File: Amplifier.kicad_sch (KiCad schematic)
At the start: 62 parts, among them Q301 PNP, Q302 NPN, Q303 PNP, Q304 NPN, Q305 NPN, Q306 PNP, Q307 NPN, Q308 PNP, Q309 PNP, Q310 NPN, Q311 PNP, Q312 NPN, Q313 PNP, Q314 NPN, Q315 PNP, Q316 NPN, Q317 NPN, Q318 PNP, Q319 NPN, Q320 PNP, Q321 PNP, Q322 NPN, Q323 PNP, Q324 NPN, U301 ???, U302 ???

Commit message: 回路図ひとまず完成
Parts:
- removed Q301, Q303, Q308, Q320, Q321, Q323: PNP, Package_TO_SOT_THT:TO-92L_Inline_Wide, symbol Transistor_BJT:Q_PNP_ECB
- removed Q304, Q305, Q307, Q317, Q319, Q324: NPN, Package_TO_SOT_THT:TO-92L_Inline_Wide, symbol Transistor_BJT:Q_NPN_ECB
- removed RV301, RV302: 10k, MyLibrary:SL4515G, symbol MysymbolLibrary:RV_2C
- added Q401, Q402, Q411, Q412, Q417, Q418: TPC6901A, symbol MysymbolLibrary:TPC6901A
- added RV401: R, MyLibrary:RV_2C, symbol MysymbolLibrary:RV_2C
- renumbered C302 to C401, C301 to C402, HS301 to HS401, HS303 to HS402, HS302 to HS403, HS304 to HS404, Q309 to Q403, Q313 to Q404, Q302 to Q405, Q322 to Q406, Q306 to Q407, Q318 to Q408, Q310 to Q409, Q314 to Q410, Q311 to Q413, Q315 to Q414, Q312 to Q415, Q316 to Q416, R307 to R401, R319 to R402, R311 to R403, R315 to R404, R312 to R405, R316 to R406, R305 to R407, R323 to R408, R308 to R409, R320 to R410, R303 to R411, R325 to R412, R301 to R413, R328 to R414, R306 to R415, R324 to R416, R302 to R417, R327 to R418, R309 to R419, R321 to R420, R304 to R421, R326 to R422, R313 to R423, R317 to R424, R314 to R425, R318 to R426, R310 to R427, R322 to R428, U301 to U401, U302 to U402
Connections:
- net EQ_L: now also RV401.1
- net EQ_R: now also RV401.4
- net GNDREF: now also RV401.3, RV401.6
- net V+: now also Q417.6, Q418.6
- net V-: now also Q401.4, Q402.4, Q411.4, Q412.4
- net at Q414.2 (C), R424.1: now also Q412.5
- net at R401.2: now also Q401.1, Q401.2
- net at R419.2: now also Q411.1, Q411.2
- net at R414.1, U402.5 (+): now also RV401.5
- net at Q406.3 (B), R408.2, U402.7: now also Q402.3
- net at Q416.2 (C), R426.2: now also Q418.2
- net at Q416.3 (B): now also Q418.4
- net at Q405.3 (B), R407.2, U401.7: now also Q401.3
- net at Q415.2 (C), R425.2: now also Q417.2
- net at Q413.2 (C), R423.1: now also Q411.5
- net at R416.2, U402.8: now also Q412.3, Q418.1
- net at R402.2: now also Q402.1, Q402.2
- net at Q404.2 (C), R404.1: now also Q402.5
- net at Q404.3 (B): now also Q402.6
- net at R428.1: now also Q418.3, Q418.5
- net at Q403.2 (C), R403.1: now also Q401.5
- net at Q403.3 (B): now also Q401.6
- net at Q415.3 (B): now also Q417.4
- net at Q413.3 (B): now also Q411.6
- net at R413.1, U401.5 (+): now also RV401.2
- net at Q414.3 (B): now also Q412.6
- net at R415.2, U401.8: now also Q411.3, Q417.1
- net at R427.1: now also Q417.3, Q417.5
- net at R420.2: now also Q412.1, Q412.2

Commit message: Amplifier回路図更新
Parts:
- removed Q405, Q406: NPN, Package_TO_SOT_THT:TO-92L_Inline_Wide, symbol Transistor_BJT:Q_NPN_ECB
- removed Q407, Q408: PNP, Package_TO_SOT_THT:TO-92L_Inline_Wide, symbol Transistor_BJT:Q_PNP_ECB
- added Q407, Q408: TPC6901A, symbol MysymbolLibrary:TPC6901A
- renumbered Q409 to Q405, Q410 to Q406, Q411 to Q409, Q412 to Q410, Q413 to Q411, Q414 to Q412, Q415 to Q413, Q416 to Q414, Q417 to Q415, Q418 to Q416
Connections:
- net V+: now also Q407.6, Q408.6
- net at Q402.3, R408.2, U402.7: now also Q408.1
- net at Q406.2 (C), R406.2: now also Q408.2
- net at Q406.3 (B): now also Q408.4
- net at R410.1: now also Q408.3, Q408.5
- net at Q401.3, R407.2, U401.7: now also Q407.1
- net at R409.1: now also Q407.3, Q407.5
- net at Q405.2 (C), R405.2: now also Q407.2
- net at Q405.3 (B): now also Q407.4

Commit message: 部品ほぼ割り当て
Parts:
- C401, C402: footprint (none) -> Capacitor_SMD:C_1206_3216Metric
- HS401, HS402, HS403, HS404: footprint (none) -> MyLibrary:17PB024
- Q401, Q402, Q407, Q408, Q409, Q410, Q415, Q416: footprint (none) -> Package_TO_SOT_SMD:SOT-23-6
- Q403, Q404, Q405, Q406, Q411, Q412, Q413, Q414: footprint Package_TO_SOT_THT:TO-92L_Inline_Wide -> Package_TO_SOT_THT:TO-126-3_Vertical
- R401, R402, R409, R410, R419, R420, R427, R428: footprint Resistor_THT:R_Axial_DIN0204_L3.6mm_D1.6mm_P5.08mm_Horizontal -> Resistor_SMD:R_2512_6332Metric
- R407, R408, R411, R412, R413, R414, R415, R416, R417, R418, R421, R422: footprint Resistor_THT:R_Axial_DIN0204_L3.6mm_D1.6mm_P5.08mm_Horizontal -> Resistor_SMD:R_0603_1608Metric
- U401, U402: footprint (none) -> Package_DIP:DIP-14_W7.62mm_Socket
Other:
- note added: "ヒートシンク"
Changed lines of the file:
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@@
 		)
 	)
+	(text "ヒートシンク"
+		(exclude_from_sim no)
+		(at 271.78 74.168 0)
+		(effects
+			(font
+				(size 1.27 1.27)
+			)
+			(href "https://akizukidenshi.com/catalog/g/g105049/")
+		)
+	)
 	(text "Rd"
 		(exclude_from_sim no)
@@
 			)
 		)
-		(property "Footprint" "Resistor_THT:R_Axial_DIN0204_L3.6mm_D1.6mm_P5.08mm_Horizontal"
+		(property "Footprint" "Resistor_SMD:R_2512_6332Metric"
 			(at 108.712 43.18 90)
 			(hide yes)
@@
 			)
 		)
-		(property "Footprint" "Resistor_THT:R_Axial_DIN0204_L3.6mm_D1.6mm_P5.08mm_Horizontal"
+		(property "Footprint" "Resistor_SMD:R_0603_1608Metric"
 			(at 76.708 106.68 90)
 			(hide yes)
@@
 			)
 		)
-		(property "Footprint" "Resistor_THT:R_Axial_DIN0204_L3.6mm_D1.6mm_P5.08mm_Horizontal"
+		(property "Footprint" "Resistor_SMD:R_2512_6332Metric"
 			(at 108.712 105.41 90)
 			(hide yes)
@@
 			)
 		)
-		(property "Footprint" ""
+		(property "Footprint" "Package_DIP:DIP-14_W7.62mm_Socket"
 			(at 251.46 25.4 0)
 			(hide yes)
@@
 			)
 		)
-		(property "Footprint" ""
+		(property "Footprint" "Package_DIP:DIP-14_W7.62mm_Socket"
 			(at 276.86 25.4 0)
 			(hide yes)
@@
 			)
 		)
-		(property "Footprint" ""
+		(property "Footprint" "Package_DIP:DIP-14_W7.62mm_Socket"
 			(at 213.36 80.01 0)
 			(hide yes)
@@
 			)
 		)
-		(property "Footprint" "Package_TO_SOT_THT:TO-92L_Inline_Wide"
+		(property "Footprint" "Package_TO_SOT_THT:TO-126-3_Vertical"
 			(at 161.29 138.43 0)
 			(hide yes)
@@
 			)
 		)
-		(property "Footprint" "Resistor_THT:R_Axial_DIN0204_L3.6mm_D1.6mm_P5.08mm_Horizontal"
+		(property "Footprint" "Resistor_SMD:R_0603_1608Metric"
 			(at 76.708 82.55 90)
 			(hide yes)
@@
 			)
 		)
-		(property "Footprint" ""
+		(property "Footprint" "Package_DIP:DIP-14_W7.62mm_Socket"
 			(at 58.42 106.68 0)
 			(hide yes)
@@
 			)
 		)
-		(property "Footprint" "Resistor_THT:R_Axial_DIN0204_L3.6mm_D1.6mm_P5.08mm_Horizontal"
+		(property "Footprint" "Resistor_SMD:R_0603_1608Metric"
 			(at 213.36 98.298 90)
 			(hide yes)
@@
 			)
 		)
-		(property "Footprint" ""
+		(property "Footprint" "Package_TO_SOT_SMD:SOT-23-6"
 			(at 124.46 82.55 0)
 			(hide yes)
@@
 			)
 		)
-		(property "Footprint" "Resistor_THT:R_Axial_DIN0204_L3.6mm_D1.6mm_P5.08mm_Horizontal"
+		(property "Footprint" "Resistor_SMD:R_0603_1608Metric"
 			(at 221.742 106.68 90)
 			(hide yes)
@@
 			)
 		)
-		(property "Footprint" "Package_TO_SOT_THT:TO-92L_Inline_Wide"
+		(property "Footprint" "Package_TO_SOT_THT:TO-126-3_Vertical"
 			(at 161.29 45.72 0)
 			(hide yes)
@@
 			)
 		)
-		(property "Footprint" "Resistor_THT:R_Axial_DIN0204_L3.6mm_D1.6mm_P5.08mm_Horizontal"
+		(property "Footprint" "Resistor_SMD:R_2512_6332Metric"
 			(at 184.658 140.97 90)
 			(hide yes)
@@
 			)
 		)
-		(property "Footprint" ""
+		(property "Footprint" "Package_TO_SOT_SMD:SOT-23-6"
 			(at 110.49 101.6 0)
 			(hide yes)
@@
 			)
 		)
-		(property "Footprint" ""
+		(property "Footprint" "Package_TO_SOT_SMD:SOT-23-6"
 			(at 124.46 144.78 0)
 			(hide yes)
@@
 			)
 		)
-		(property "Footprint" "Package_TO_SOT_THT:TO-92L_Inline_Wide"
+		(property "Footprint" "Package_TO_SOT_THT:TO-126-3_Vertical"
 			(at 132.08 45.72 0)
 			(hide yes)
@@
 			)
 		)
-		(property "Footprint" ""
+		(property "Footprint" "Package_TO_SOT_SMD:SOT-23-6"
 			(at 110.49 39.37 0)
 			(hide yes)
@@
 			)
 		)
-		(property "Footprint" "Package_TO_SOT_THT:TO-92L_Inline_Wide"
+		(property "Footprint" "Package_TO_SOT_THT:TO-126-3_Vertical"
 			(at 132.08 138.43 0)
 			(hide yes)
@@
 			)
 		)
-		(property "Footprint" "Package_TO_SOT_THT:TO-92L_Inline_Wide"
+		(property "Footprint" "Package_TO_SOT_THT:TO-126-3_Vertical"
 			(at 132.08 107.95 0)
 			(hide yes)
@@
 			)
 		)
-		(property "Footprint" "Resistor_THT:R_Axial_DIN0204_L3.6mm_D1.6mm_P5.08mm_Horizontal"
+		(property "Footprint" "Resistor_SMD:R_0603_1608Metric"
 			(at 221.742 82.55 90)
 			(hide yes)
@@
 			)
 		)
-		(property "Footprint" "Resistor_THT:R_Axial_DIN0204_L3.6mm_D1.6mm_P5.08mm_Horizontal"
+		(property "Footprint" "Resistor_SMD:R_0603_1608Metric"
 			(at 85.09 74.168 90)
 			(hide yes)
@@
 			)
 		)
-		(property "Footprint" "Resistor_THT:R_Axial_DIN0204_L3.6mm_D1.6mm_P5.08mm_Horizontal"
+		(property "Footprint" "Resistor_SMD:R_0603_1608Metric"
 			(at 52.578 93.98 90)
 			(hide yes)
@@
 			)
 		)
-		(property "Footprint" "Package_TO_SOT_THT:TO-92L_Inline_Wide"
+		(property "Footprint" "Package_TO_SOT_THT:TO-126-3_Vertical"
 			(at 161.29 107.95 0)
 			(hide yes)
@@
 			)
 		)
-		(property "Footprint" ""
+		(property "Footprint" "Package_DIP:DIP-14_W7.62mm_Socket"
 			(at 248.92 49.53 0)
 			(hide yes)
@@
 			)
 		)
-		(property "Footprint" "Resistor_THT:R_Axial_DIN0204_L3.6mm_D1.6mm_P5.08mm_Horizontal"
+		(property "Footprint" "Resistor_SMD:R_0603_1608Metric"
 			(at 240.03 100.838 90)
 			(hide yes)
@@
 			)
 		)
-		(property "Footprint" "Package_TO_SOT_THT:TO-92L_Inline_Wide"
+		(property "Footprint" "Package_TO_SOT_THT:TO-126-3_Vertical"
 			(at 161.29 76.2 0)
 			(hide yes)
@@
 			)
 		)
-		(property "Footprint" ""
+		(property "Footprint" "Package_TO_SOT_SMD:SOT-23-6"
 			(at 182.88 39.37 0)
 			(hide yes)
@@
 			)
 		)
-		(property "Footprint" ""
+		(property "Footprint" "Package_TO_SOT_SMD:SOT-23-6"
 			(at 182.88 101.6 0)
 			(hide yes)
@@
 			)
 		)
-		(property "Footprint" ""
+		(property "Footprint" "MyLibrary:17PB024"
 			(at 269.5448 69.85 0)
 			(hide yes)
@@
 			)
 		)
-		(property "Footprint" "Resistor_THT:R_Axial_DIN0204_L3.6mm_D1.6mm_P5.08mm_Horizontal"
+		(property "Footprint" "Resistor_SMD:R_0603_1608Metric"
 			(at 213.36 74.168 90)
 			(hide yes)
@@
 			)
 		)
-		(property "Footprint" "Resistor_THT:R_Axial_DIN0204_L3.6mm_D1.6mm_P5.08mm_Horizontal"
+		(property "Footprint" "Resistor_SMD:R_0603_1608Metric"
 			(at 85.09 98.298 90)
 			(hide yes)
@@
 			)
 		)
-		(property "Footprint" ""
+		(property "Footprint" "MyLibrary:17PB024"
 			(at 251.7648 69.85 0)
 			(hide yes)
@@
 			)
 		)
-		(property "Footprint" ""
+		(property "Footprint" "Package_TO_SOT_SMD:SOT-23-6"
 			(at 168.91 144.78 0)
 			(hide yes)
@@
 			)
 		)
-		(property "Footprint" "Resistor_THT:R_Axial_DIN0204_L3.6mm_D1.6mm_P5.08mm_Horizontal"
+		(property "Footprint" "Resistor_SMD:R_0603_1608Metric"
 			(at 58.42 100.838 90)
 			(hide yes)
@@
 			)
 		)
-		(property "Footprint" ""
+		(property "Footprint" "Package_DIP:DIP-14_W7.62mm_Socket"
 			(at 240.03 106.68 0)
 			(hide yes)
@@
 			)
 		)
-		(property "Footprint" "Resistor_THT:R_Axial_DIN0204_L3.6mm_D1.6mm_P5.08mm_Horizontal"
+		(property "Footprint" "Resistor_SMD:R_2512_6332Metric"
 			(at 184.658 43.18 90)
 			(hide yes)
@@
 			)
 		)
-		(property "Footprint" ""
+		(property "Footprint" "Capacitor_SMD:C_1206_3216Metric"
 			(at 246.0752 29.21 0)
 			(hide yes)
@@
 			)
 		)
-		(property "Footprint" "Resistor_THT:R_Axial_DIN0204_L3.6mm_D1.6mm_P5.08mm_Horizontal"
+		(property "Footprint" "Resistor_SMD:R_2512_6332Metric"
 			(at 184.658 78.74 90)
 			(hide yes)
@@
 			)
 		)
-		(property "Footprint" "Resistor_THT:R_Axial_DIN0204_L3.6mm_D1.6mm_P5.08mm_Horizontal"
+		(property "Footprint" "Resistor_SMD:R_2512_6332Metric"
 			(at 108.712 78.74 90)
 			(hide yes)
@@
 			)
 		)
-		(property "Footprint" ""
+		(property "Footprint" "Package_DIP:DIP-14_W7.62mm_Socket"
 			(at 213.36 104.14 0)
 			(hide yes)
@@
 			)
 		)
-		(property "Footprint" "Resistor_THT:R_Axial_DIN0204_L3.6mm_D1.6mm_P5.08mm_Horizontal"
+		(property "Footprint" "Resistor_SMD:R_2512_6332Metric"
 			(at 108.712 140.97 90)
 			(hide yes)
@@
 			)
 		)
-		(property "Footprint" ""
+		(property "Footprint" "MyLibrary:17PB024"
 			(at 251.7648 64.77 0)
 			(hide yes)
@@
 			)
 		)
-		(property "Footprint" ""
+		(property "Footprint" "Capacitor_SMD:C_1206_3216Metric"
 			(at 271.4752 29.21 0)
 			(hide yes)
@@
 			)
 		)
-		(property "Footprint" ""
+		(property "Footprint" "Package_DIP:DIP-14_W7.62mm_Socket"
 			(at 274.32 49.53 0)
 			(hide yes)
@@
 			)
 		)
-		(property "Footprint" "Resistor_THT:R_Axial_DIN0204_L3.6mm_D1.6mm_P5.08mm_Horizontal"
+		(property "Footprint" "Resistor_SMD:R_2512_6332Metric"
 			(at 184.658 105.41 90)
 			(hide yes)
@@
 			)
 		)
-		(property "Footprint" ""
+		(property "Footprint" "Package_TO_SOT_SMD:SOT-23-6"
 			(at 168.91 82.55 0)
 			(hide yes)
@@
 			)
 		)
-		(property "Footprint" ""
+		(property "Footprint" "Package_DIP:DIP-14_W7.62mm_Socket"
 			(at 85.09 80.01 0)
 			(hide yes)
@@
 			)
 		)
-		(property "Footprint" ""
+		(property "Footprint" "Package_DIP:DIP-14_W7.62mm_Socket"
 			(at 85.09 104.14 0)
 			(hide yes)
@@
 			)
 		)
-		(property "Footprint" ""
+		(property "Footprint" "MyLibrary:17PB024"
 			(at 269.5448 64.77 0)
 			(hide yes)
@@
 			)
 		)
-		(property "Footprint" "Package_TO_SOT_THT:TO-92L_Inline_Wide"
+		(property "Footprint" "Package_TO_SOT_THT:TO-126-3_Vertical"
 			(at 132.08 76.2 0)
 			(hide yes)
@@
 			)
 		)
-		(property "Footprint" "Resistor_THT:R_Axial_DIN0204_L3.6mm_D1.6mm_P5.08mm_Horizontal"
+		(property "Footprint" "Resistor_SMD:R_0603_1608Metric"
 			(at 245.872 93.98 90)
 			(hide yes)

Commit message: 部品配置すすめた
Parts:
- removed HS401, HS402, HS403, HS404: Heatsink, MyLibrary:17PB024, symbol Mechanical:Heatsink
- Q403, Q404, Q411, Q412: value PNP -> 2SA1359
- Q405, Q406, Q413, Q414: value NPN -> 2SC3422
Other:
- note added: "100~200mAくらい"
- note added: "やっぱヒートシンクこれで 長い一体のもの，8℃/W ダメだったら空冷で"

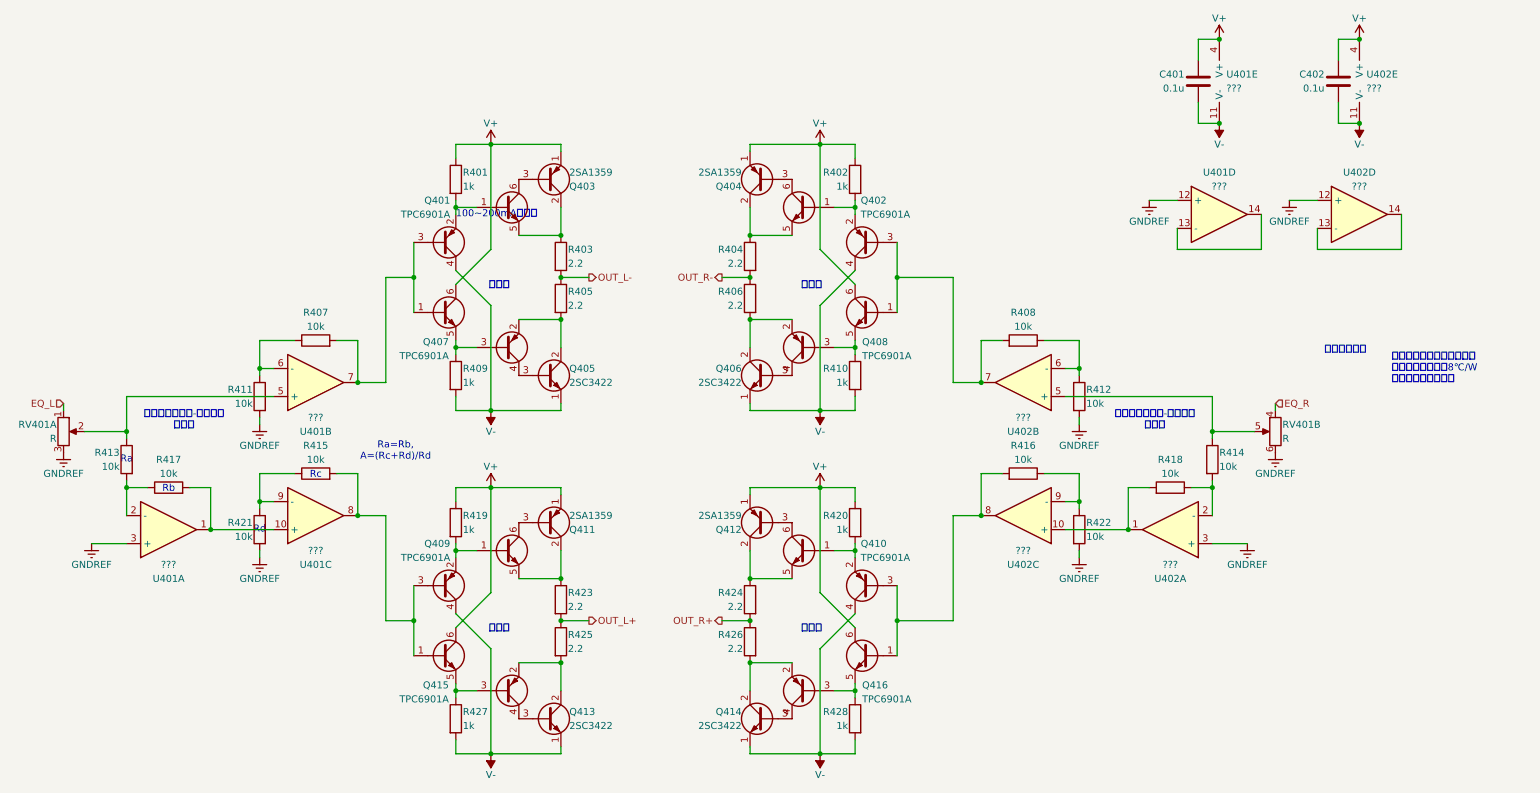
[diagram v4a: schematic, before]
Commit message: 回路図一部変更，部品ほぼ置いた　寝かせる
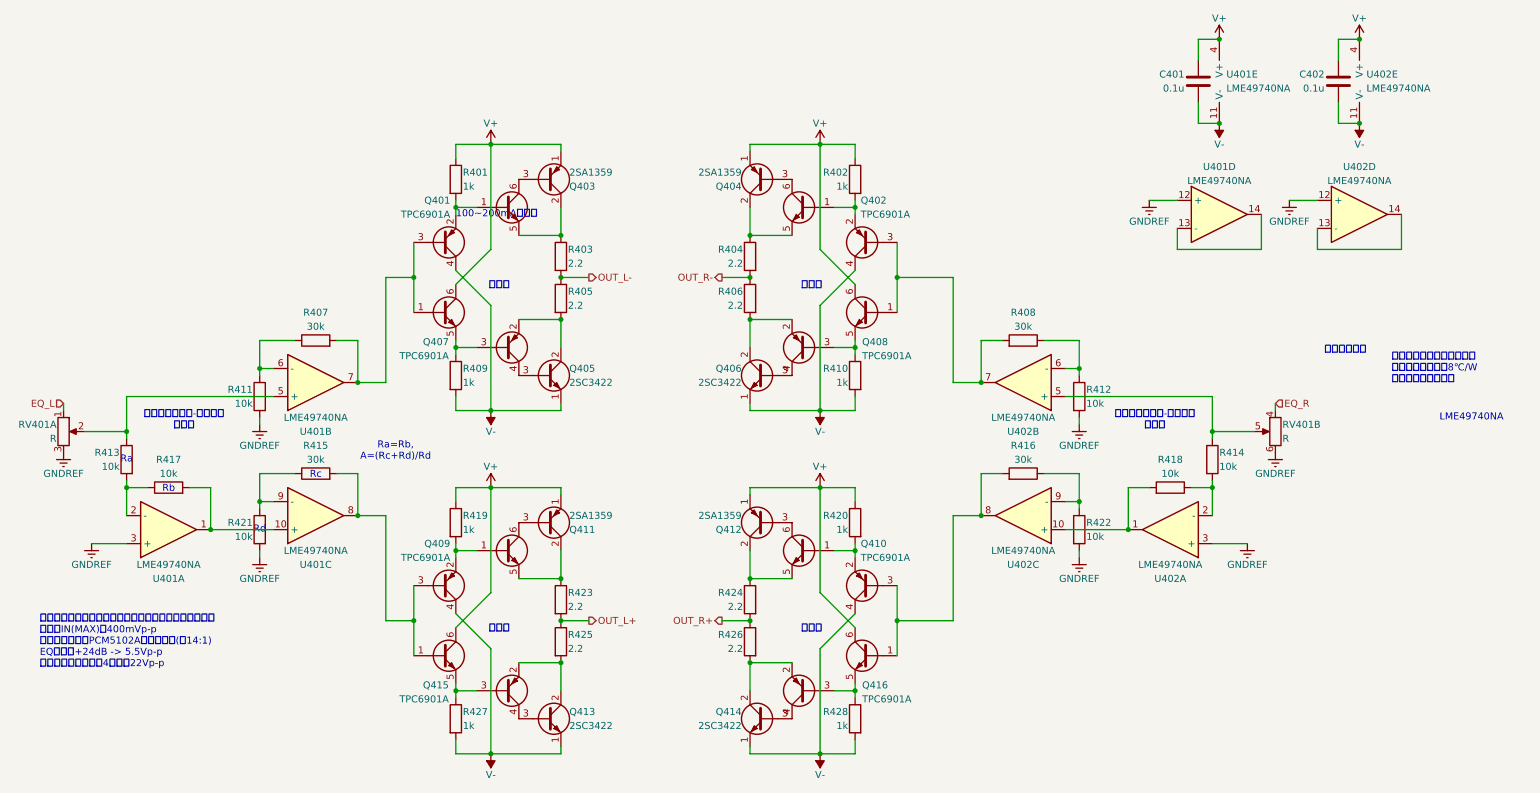
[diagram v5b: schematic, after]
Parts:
- R407, R408, R415, R416: value 10k -> 30k
- U401, U402: value ??? -> LME49740NA
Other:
- note added: "LME49740NA"
- note added: "最大電圧，最大ボリュームでクリップしないように設定 ラインIN(MAX)：400mVp-p これに合わせてPCM5102A出力も分圧(約14:1) EQで最大+24dB -> 5.5Vp-p これを電圧増幅段で4倍して22Vp-p"
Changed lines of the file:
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@@
 		)
 	)
+	(text "最大電圧，最大ボリュームでクリップしないように設定\nラインIN(MAX)：400mVp-p\nこれに合わせてPCM5102A出力も分圧(約14:1)\nEQで最大+24dB -> 5.5Vp-p\nこれを電圧増幅段で4倍して22Vp-p"
+		(exclude_from_sim no)
+		(at 35.052 127 0)
+		(effects
+			(font
+				(size 1.27 1.27)
+			)
+			(justify left)
+		)
+	)
 	(text "Rd"
 		(exclude_from_sim no)
@@
 		)
 	)
+	(text "LME49740NA"
+		(exclude_from_sim no)
+		(at 294.64 86.36 0)
+		(effects
+			(font
+				(size 1.27 1.27)
+			)
+			(href "https://akizukidenshi.com/catalog/g/g103685/")
+		)
+	)
 	(junction
 		(at 74.93 77.47)
@@
 			)
 		)
-		(property "Value" "???"
+		(property "Value" "LME49740NA"
 			(at 250.19 26.6699 0)
 			(show_name no)
@@
 			)
 		)
-		(property "Value" "???"
+		(property "Value" "LME49740NA"
 			(at 275.59 26.6699 0)
 			(show_name no)
@@
 			)
 		)
-		(property "Value" "???"
+		(property "Value" "LME49740NA"
 			(at 213.36 86.36 0)
 			(show_name no)
@@
 			)
 		)
-		(property "Value" "???"
+		(property "Value" "LME49740NA"
 			(at 58.42 113.03 0)
 			(show_name no)
@@
 			)
 		)
-		(property "Value" "10k"
+		(property "Value" "30k"
 			(at 213.36 93.98 90)
 			(show_name no)
@@
 			)
 		)
-		(property "Value" "10k"
+		(property "Value" "30k"
 			(at 85.09 69.85 90)
 			(show_name no)
@@
 		(dnp no)
 		(property "Reference" "U401"
-			(at 248.92 41.91 0)
+			(at 248.92 40.894 0)
 			(show_name no)
 			(do_not_autoplace no)
@@
 			)
 		)
-		(property "Value" "???"
-			(at 248.92 44.45 0)
+		(property "Value" "LME49740NA"
+			(at 248.92 43.434 0)
 			(show_name no)
 			(do_not_autoplace no)
@@
 			)
 		)
-		(property "Value" "10k"
+		(property "Value" "30k"
 			(at 213.36 69.85 90)
 			(show_name no)
@@
 			)
 		)
-		(property "Value" "10k"
+		(property "Value" "30k"
 			(at 85.09 93.98 90)
 			(show_name no)
@@
 			)
 		)
-		(property "Value" "???"
+		(property "Value" "LME49740NA"
 			(at 240.03 113.03 0)
 			(show_name no)
@@
 			)
 		)
-		(property "Value" "???"
+		(property "Value" "LME49740NA"
 			(at 213.36 110.49 0)
 			(show_name no)
@@
 		(dnp no)
 		(property "Reference" "U402"
-			(at 274.32 41.91 0)
+			(at 274.32 40.894 0)
 			(show_name no)
 			(do_not_autoplace no)
@@
 			)
 		)
-		(property "Value" "???"
-			(at 274.32 44.45 0)
+		(property "Value" "LME49740NA"
+			(at 274.32 43.434 0)
 			(show_name no)
 			(do_not_autoplace no)
@@
 			)
 		)
-		(property "Value" "???"
+		(property "Value" "LME49740NA"
 			(at 85.09 86.36 0)
 			(show_name no)
@@
 			)
 		)
-		(property "Value" "???"
+		(property "Value" "LME49740NA"
 			(at 85.09 110.49 0)
 			(show_name no)
